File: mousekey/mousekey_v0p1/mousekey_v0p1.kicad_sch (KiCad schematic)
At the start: 0 parts

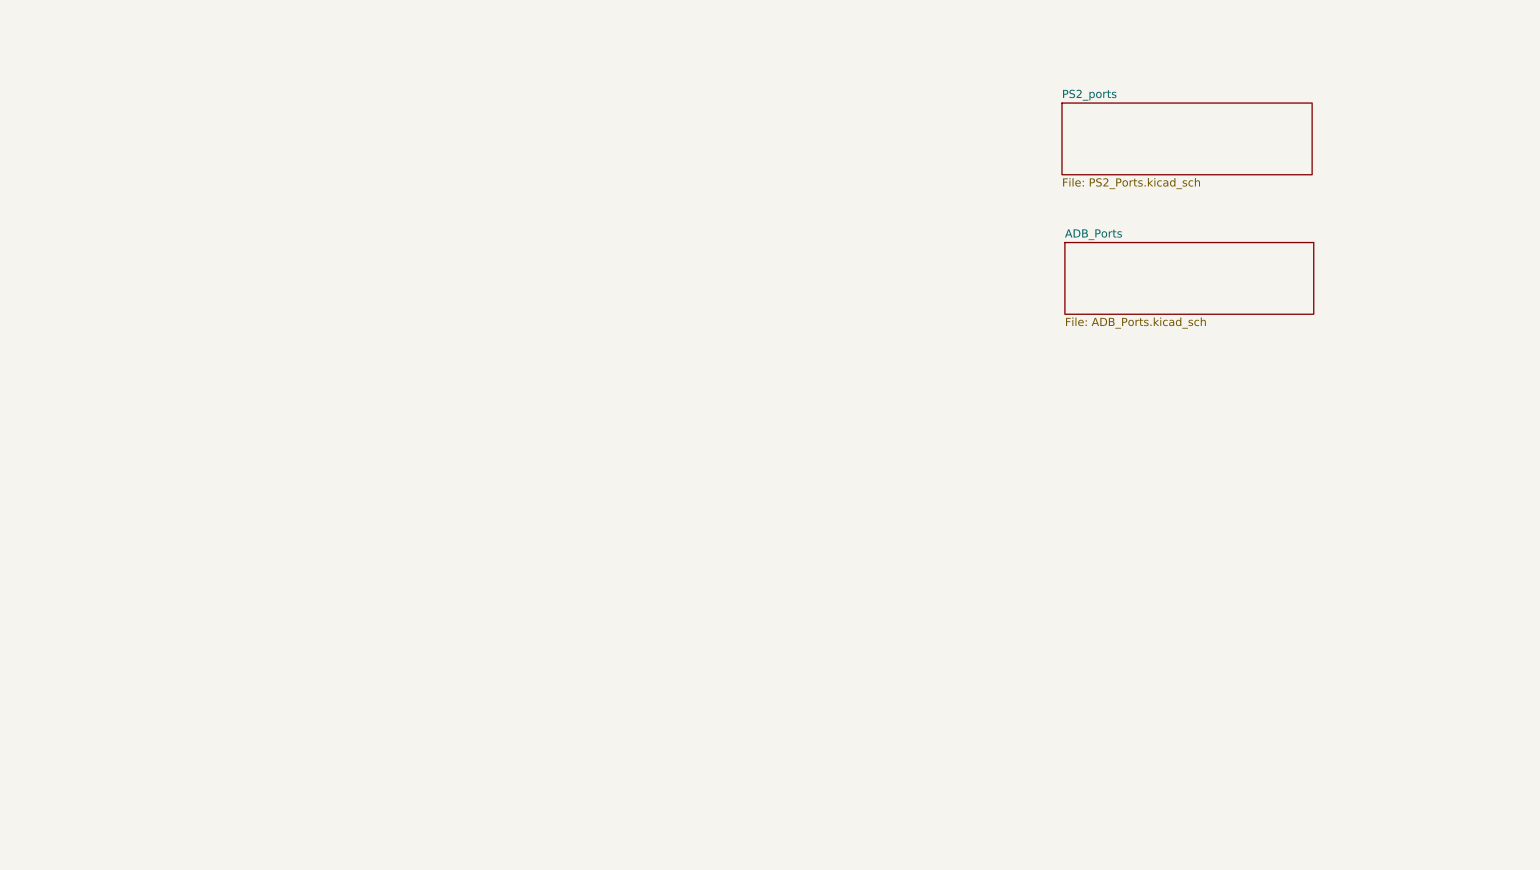
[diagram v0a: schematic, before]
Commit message: Added ADB and Teensy
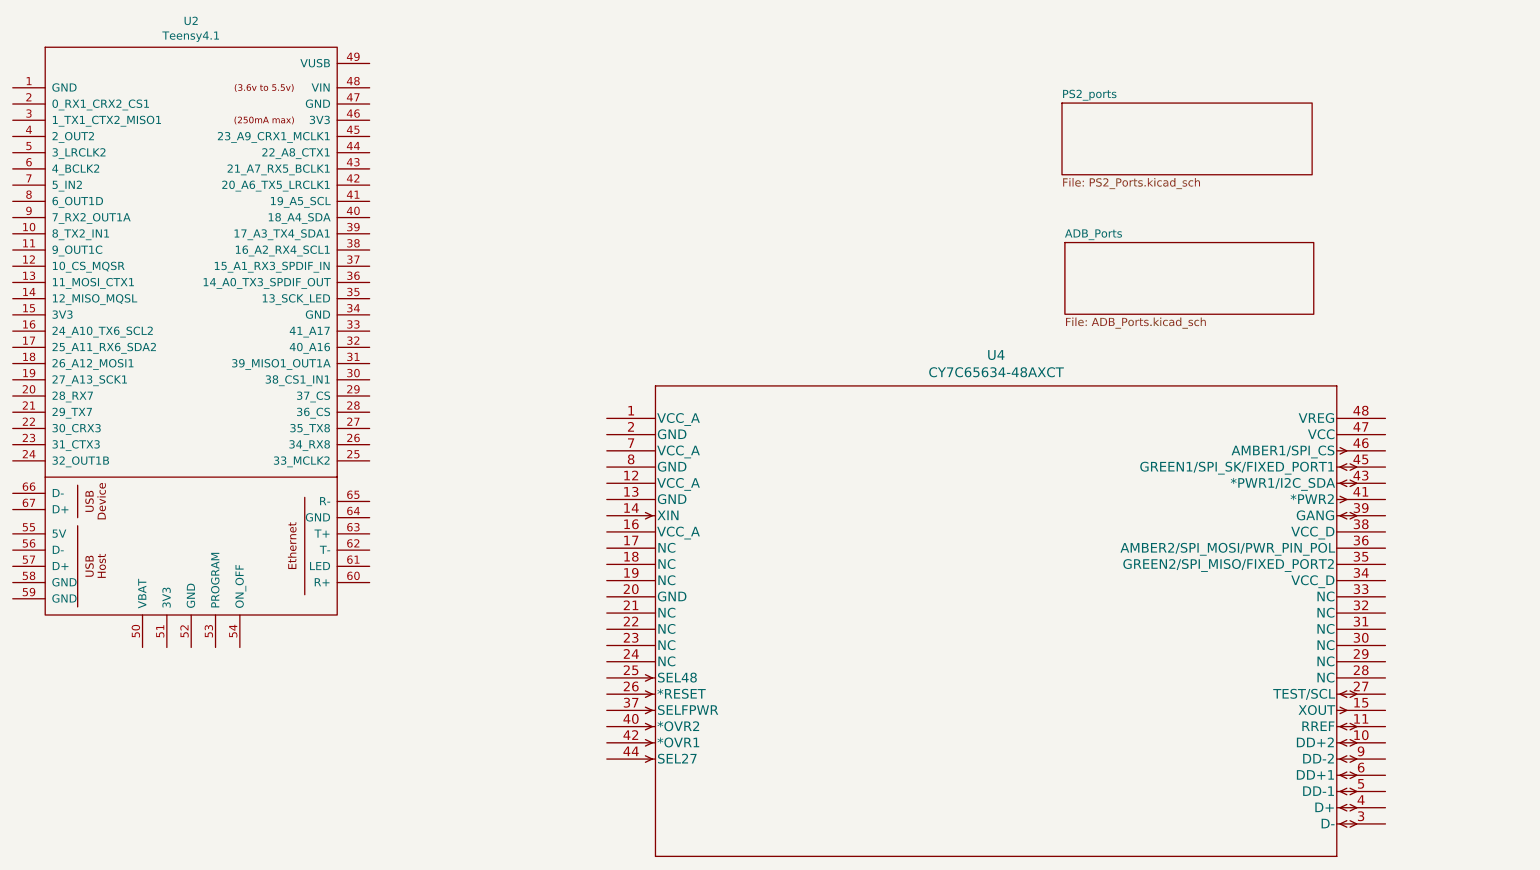
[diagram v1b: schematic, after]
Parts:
- added U2: Teensy4.1, teensy:Teensy41, symbol teensy:Teensy4.1
- added U4: CY7C65634-48AXCT, teensy:CY7C65634-48AXCT, symbol 2021-02-10_03-52-52:CY7C65634-48AXCT

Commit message: updates
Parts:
- added J? (x2): USB_A, symbol Connector:USB_A
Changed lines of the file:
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@@
   (page 1 3)
   (paper "A4")
+  (symbol (lib_id "Connector:USB_A") (at 262.9916 59.8424 0) (unit 1)
+    (in_bom yes) (on_board yes)
+    (property "Reference" "J?" (id 0) (at 264.3886 48.0122 0))
+    (property "Value" "USB_A" (id 1) (at 264.3886 50.3109 0))
+    (property "Footprint" "" (id 2) (at 266.8016 61.1124 0)
+      (effects (font (size 1.27 1.27)) hide)
+    )
+    (property "Datasheet" " ~" (id 3) (at 266.8016 61.1124 0)
+      (effects (font (size 1.27 1.27)) hide)
+    )
+  )
+  (symbol (lib_id "Connector:USB_A") (at 265.5824 86.9696 0) (unit 1)
+    (in_bom yes) (on_board yes)
+    (property "Reference" "J?" (id 0) (at 266.9794 75.1394 0))
+    (property "Value" "USB_A" (id 1) (at 266.9794 77.4381 0))
+    (property "Footprint" "" (id 2) (at 269.3924 88.2396 0)
+      (effects (font (size 1.27 1.27)) hide)
+    )
+    (property "Datasheet" " ~" (id 3) (at 269.3924 88.2396 0)
+      (effects (font (size 1.27 1.27)) hide)
+    )
+  )
   (symbol (lib_id "teensy:Teensy4.1") (at 64.008 87.2236 0) (unit 1)
     (in_bom yes) (on_board yes)
@@
   )
   (symbol_instances
+    (path "/0b7c8e5c-6c5a-4d20-8e35-54b083634a88"
+      (reference "J?") (unit 1) (value "USB_A") (footprint "")
+    )
+    (path "/60e6d27a-3169-4b93-9f2b-7812bff67b83"
+      (reference "J?") (unit 1) (value "USB_A") (footprint "")
+    )
     (path "/b1f7cdce-c92f-41bb-ba75-9cb3d872bb46"
       (reference "U2") (unit 1) (value "Teensy4.1") (footprint "teensy:Teensy41")

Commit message: updates
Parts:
- removed J? (x2): USB_A, symbol Connector:USB_A
- removed U4: CY7C65634-48AXCT, teensy:CY7C65634-48AXCT, symbol 2021-02-10_03-52-52:CY7C65634-48AXCT
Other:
- added sheet RS-232 (RS-232_Ports.kicad_sch)
- added sheet USB Hub and Ports (USB_Hub_And_Ports.kicad_sch)
